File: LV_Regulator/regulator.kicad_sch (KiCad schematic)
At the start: 0 parts

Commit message: Kicad Regulator & Buck Boost controller Schematic Progress
Put down basic components and imported TI FET's & Buck-Boost Controller, as well as some of the basic connections between Controller and FET's.
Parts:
- added C1, C2: 100, symbol Device:C
- added C3: 80uF, symbol Device:C
- added C4: 40uF, symbol Device:C
- added L1: 10uH, symbol Device:L
- added R5: 133k, symbol Device:R
- added U1: BQ25858QWRRVRQ1, RRV0036B-IPC_A, symbol Controller_Library:BQ25858QWRRVRQ1
- added U2, U3, U4, U5: CSD19506KTT, DDPAK/TO-263_KTT_TEX, symbol Controller_Library:CSD19506KTT
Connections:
- new net: C1.2, U1.26 (BTST1)
- new net: C4.1, U4.2 (D)
- new net: R5.1, U1.36 (FSW_SYNC)
- new net BTST2: C2.2, U1.20 (BTST2)
- new net GND: C3.2, C4.2, R5.2, U1.10 (IIN), U1.17 (MODE), U1.37 (PGND), U1.9 (IOUT), U3.3 (S), U5.3 (S)
- new net HIDRV1_FET1_U2: U1.27 (HIDRV1), U2.1 (G)
- new net HIDRV2_FET4_U4: U1.19 (HIDRV2), U4.1 (G)
- new net LODRV1_FET2_U5: U1.25 (LODRV1), U5.1 (G)
- new net LODRV2_FET3_U3: U1.21 (LODRV2), U3.1 (G)
- new net SW1_FETs: C1.1, L1.1, U1.28 (SW1), U2.3 (S), U5.2 (D)
- new net SW2-FETs: C2.1, L1.2, U1.18 (SW2), U3.2 (D), U4.3 (S)
- new net VAC: C3.1, U2.2 (D)
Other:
- note added: "Buck-Boost Controller"
- note added: "MOSFET's & VAC wiring"

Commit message: Fixed last commit
Fixed all mistakes from the last push
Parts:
- removed C1, C2: 100, symbol Device:C
- removed C3: 80uF, symbol Device:C
- removed C4: 40uF, symbol Device:C
- added C20: 80uF, symbol Device:C
- added C21, C24: 40uF, symbol Device:C
- added C22, C23, C25, C26: 100nF, symbol Device:C
- added C27: C_Polarized, symbol Device:C_Polarized
- added R10: 5m, symbol Device:R
- added R11, R12: 10, symbol Device:R
- renumbered R5 to R13, U4 to U10, U1 to U6, U2 to U7, U5 to U8, U3 to U9
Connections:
- net VAC is gone; now on net DCIN: U7.2 (D)
- net BTST2: now also C23.1; no longer U6.20 (BTST2)
- net GND: now also R13.1, C20.2, C21.2, C24.2, C25.1, C26.2, C27.2; no longer R13.2
- net at U6.26 (BTST1): no longer names the net of U6.26 (BTST1)
- net at U10.2 (D): now also C21.1, R10.1, R11.1
- net at U6.36 (FSW_SYNC): now also R13.2; no longer R13.1
- net I2C_SCL: now reaches U6.1 (SCL)
- net VOUT: now reaches U6.12 (VO_SNS)
- net VOUT: now also C24.1, C27.1, R10.2, R12.1
- net SRN: now reaches U6.13 (SRN)
- net SRN: now also C25.2, R12.2
- net SRP: now reaches U6.14 (SRP)
- net SRP: now also C26.1, R11.2
- net I2C_SDA: now reaches U6.2 (SDA)
- net DCIN: now reaches U6.33 (VAC)
- net DCIN: now also C20.1
- net HIDRV1_FET1_U2: no longer names the net of U6.27 (HIDRV1)
- net HIDRV1_FET1_U2: no longer U7.1 (G)
- net HIDRV2_FET4_U4: no longer names the net of U6.19 (HIDRV2)
- net HIDRV2_FET4_U4: no longer U10.1 (G)
- net LODRV1_FET2_U5: no longer names the net of U6.25 (LODRV1)
- net LODRV1_FET2_U5: no longer U8.1 (G)
- net LODRV2_FET3_U3: no longer names the net of U6.21 (LODRV2)
- net LODRV2_FET3_U3: no longer U9.1 (G)
- net SW1_FETs renamed SW1
- net SW1: now also C22.2; no longer U6.28 (SW1)
- net SW2-FETs renamed SW2
- net SW2: now also C23.2; no longer U6.18 (SW2)
- new net BTST1: C22.1
- new net HIDRV1_FET1: U7.1 (G)
- new net HIDRV2_FET4: U10.1 (G)
- new net LODRV1_FET2: U8.1 (G)
- new net LODRV2_FET3: U9.1 (G)
- no-connect marks 0 -> 6
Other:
- note added: "MOSFET's & DCIN"
- note removed: "MOSFET's & VAC wiring"
- moved on the sheet: R13, U10, U6, U7, U8, U9

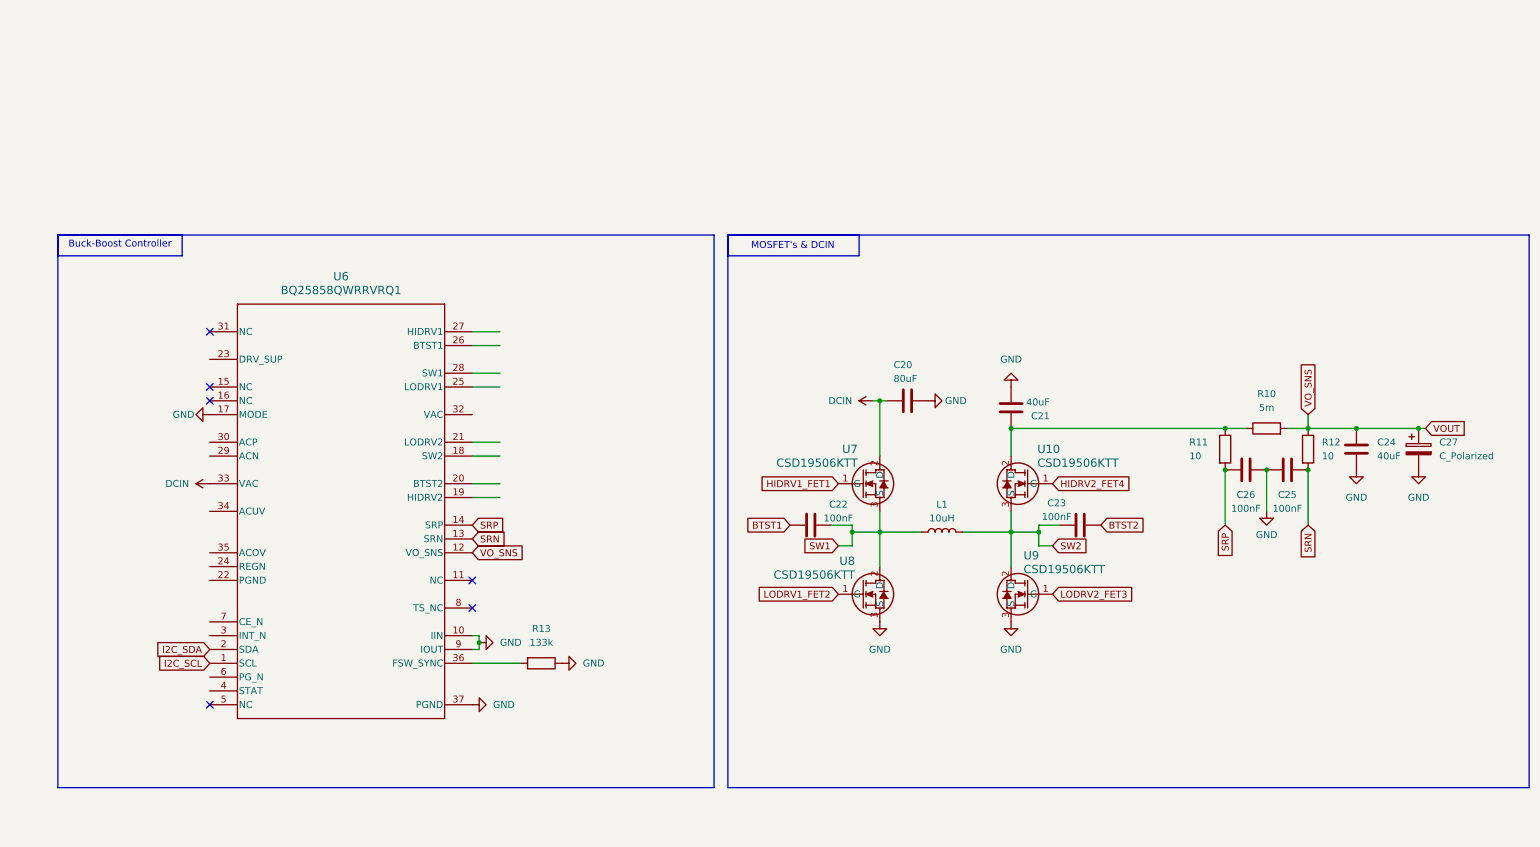
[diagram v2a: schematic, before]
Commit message: Added Start Control
Added Start Control MCU to the LV_Kontrola_Main, added hsc/lsc to LV_Regulator, fixed component numbering
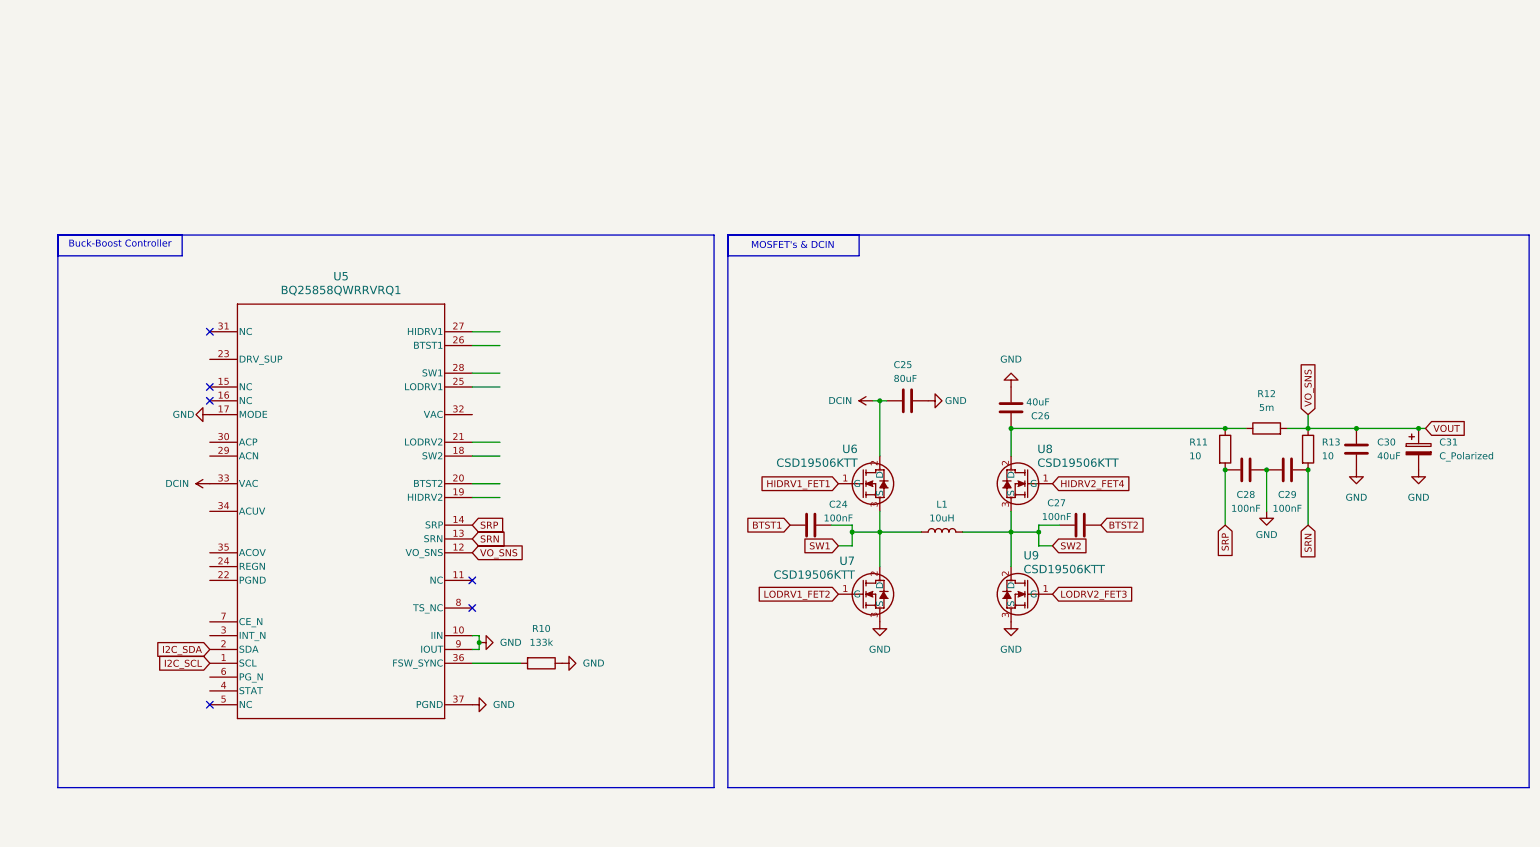
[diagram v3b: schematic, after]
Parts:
- renumbered C22 to C24, C20 to C25, C21 to C26, C23 to C27, C26 to C28, C25 to C29, C24 to C30, C27 to C31, R13 to R10, R10 to R12, R12 to R13, U6 to U5, U7 to U6, U8 to U7, U10 to U8
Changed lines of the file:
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@@
 		(dnp no)
 		(fields_autoplaced yes)
-		(property "Reference" "#PWR060"
+		(property "Reference" "#PWR066"
 			(at 44.45 99.06 0)
 			(effects
@@
 			(project ""
 				(path "/9003ce10-3354-47c9-924a-fd038a206791/7dfce8f1-0c22-480c-91d4-3ffb0e2b2dff"
-					(reference "#PWR060")
+					(reference "#PWR066")
 					(unit 1)
 				)
@@
 		(dnp no)
 		(fields_autoplaced yes)
-		(property "Reference" "#PWR059"
+		(property "Reference" "#PWR070"
 			(at 166.37 83.82 0)
 			(effects
@@
 			(project "LV_Regulator"
 				(path "/9003ce10-3354-47c9-924a-fd038a206791/7dfce8f1-0c22-480c-91d4-3ffb0e2b2dff"
-					(reference "#PWR059")
+					(reference "#PWR070")
 					(unit 1)
 				)
@@
 		(on_board yes)
 		(dnp no)
-		(property "Reference" "C21"
+		(property "Reference" "C26"
 			(at 195.072 86.614 0)
 			(effects
@@
 			(project "LV_Regulator"
 				(path "/9003ce10-3354-47c9-924a-fd038a206791/7dfce8f1-0c22-480c-91d4-3ffb0e2b2dff"
-					(reference "C21")
+					(reference "C26")
 					(unit 1)
 				)
@@
 		(dnp no)
 		(fields_autoplaced yes)
-		(property "Reference" "#PWR072"
+		(property "Reference" "#PWR073"
 			(at 187.96 74.93 0)
 			(effects
@@
 			(project "LV_Regulator"
 				(path "/9003ce10-3354-47c9-924a-fd038a206791/7dfce8f1-0c22-480c-91d4-3ffb0e2b2dff"
-					(reference "#PWR072")
+					(reference "#PWR073")
 					(unit 1)
 				)
@@
 		(on_board yes)
 		(dnp no)
-		(property "Reference" "U8"
+		(property "Reference" "U7"
 			(at 159.258 113.284 0)
 			(effects
@@
 			(project "LV_Regulator"
 				(path "/9003ce10-3354-47c9-924a-fd038a206791/7dfce8f1-0c22-480c-91d4-3ffb0e2b2dff"
-					(reference "U8")
+					(reference "U7")
 					(unit 1)
 				)
@@
 		(dnp no)
 		(fields_autoplaced yes)
-		(property "Reference" "R10"
+		(property "Reference" "R12"
 			(at 234.95 82.55 90)
 			(effects
@@
 			(project ""
 				(path "/9003ce10-3354-47c9-924a-fd038a206791/7dfce8f1-0c22-480c-91d4-3ffb0e2b2dff"
-					(reference "R10")
+					(reference "R12")
 					(unit 1)
 				)
@@
 		(on_board yes)
 		(dnp no)
-		(property "Reference" "C27"
+		(property "Reference" "C31"
 			(at 266.7 91.44 0)
 			(effects
@@
 			(project ""
 				(path "/9003ce10-3354-47c9-924a-fd038a206791/7dfce8f1-0c22-480c-91d4-3ffb0e2b2dff"
-					(reference "C27")
+					(reference "C31")
 					(unit 1)
 				)
@@
 		(on_board yes)
 		(dnp no)
-		(property "Reference" "#PWR063"
+		(property "Reference" "#PWR075"
 			(at 234.95 110.49 0)
 			(effects
@@
 			(project "LV_Regulator"
 				(path "/9003ce10-3354-47c9-924a-fd038a206791/7dfce8f1-0c22-480c-91d4-3ffb0e2b2dff"
-					(reference "#PWR063")
+					(reference "#PWR075")
 					(unit 1)
 				)
@@
 		(on_board yes)
 		(dnp no)
-		(property "Reference" "C20"
+		(property "Reference" "C25"
 			(at 166.37 77.216 90)
 			(effects
@@
 			(project ""
 				(path "/9003ce10-3354-47c9-924a-fd038a206791/7dfce8f1-0c22-480c-91d4-3ffb0e2b2dff"
-					(reference "C20")
+					(reference "C25")
 					(unit 1)
 				)
@@
 		(dnp no)
 		(fields_autoplaced yes)
-		(property "Reference" "#PWR068"
+		(property "Reference" "#PWR067"
 			(at 95.25 139.7 0)
 			(effects
@@
 			(project "LV_Regulator"
 				(path "/9003ce10-3354-47c9-924a-fd038a206791/7dfce8f1-0c22-480c-91d4-3ffb0e2b2dff"
-					(reference "#PWR068")
+					(reference "#PWR067")
 					(unit 1)
 				)
@@
 		(on_board yes)
 		(dnp no)
-		(property "Reference" "U10"
+		(property "Reference" "U8"
 			(at 192.786 92.71 0)
 			(effects
@@
 			(project "LV_Regulator"
 				(path "/9003ce10-3354-47c9-924a-fd038a206791/7dfce8f1-0c22-480c-91d4-3ffb0e2b2dff"
-					(reference "U10")
+					(reference "U8")
 					(unit 1)
 				)
@@
 		(on_board yes)
 		(dnp no)
-		(property "Reference" "#PWR066"
+		(property "Reference" "#PWR065"
 			(at 34.29 86.36 0)
 			(effects
@@
 			(project "LV_Regulator"
 				(path "/9003ce10-3354-47c9-924a-fd038a206791/7dfce8f1-0c22-480c-91d4-3ffb0e2b2dff"
-					(reference "#PWR066")
+					(reference "#PWR065")
 					(unit 1)
 				)
@@
 		(dnp no)
 		(fields_autoplaced yes)
-		(property "Reference" "#PWR062"
+		(property "Reference" "#PWR076"
 			(at 251.46 102.87 0)
 			(effects
@@
 			(project "LV_Regulator"
 				(path "/9003ce10-3354-47c9-924a-fd038a206791/7dfce8f1-0c22-480c-91d4-3ffb0e2b2dff"
-					(reference "#PWR062")
+					(reference "#PWR076")
 					(unit 1)
 				)
@@
 		(dnp no)
 		(fields_autoplaced yes)
-		(property "Reference" "R13"
+		(property "Reference" "R10"
 			(at 101.6 125.73 90)
 			(effects
@@
 			(project "LV_Regulator"
 				(path "/9003ce10-3354-47c9-924a-fd038a206791/7dfce8f1-0c22-480c-91d4-3ffb0e2b2dff"
-					(reference "R13")
+					(reference "R10")
 					(unit 1)
 				)
@@
 		(dnp no)
 		(fields_autoplaced yes)
-		(property "Reference" "#PWR070"
+		(property "Reference" "#PWR071"
 			(at 163.83 130.81 0)
 			(effects
@@
 			(project "LV_Regulator"
 				(path "/9003ce10-3354-47c9-924a-fd038a206791/7dfce8f1-0c22-480c-91d4-3ffb0e2b2dff"
-					(reference "#PWR070")
+					(reference "#PWR071")
 					(unit 1)
 				)
@@
 		(on_board yes)
 		(dnp no)
-		(property "Reference" "C23"
+		(property "Reference" "C27"
 			(at 196.342 102.616 90)
 			(effects
@@
 			(project "LV_Regulator"
 				(path "/9003ce10-3354-47c9-924a-fd038a206791/7dfce8f1-0c22-480c-91d4-3ffb0e2b2dff"
-					(reference "C23")
+					(reference "C27")
 					(unit 1)
 				)
@@
 		(dnp no)
 		(fields_autoplaced yes)
-		(property "Reference" "U6"
+		(property "Reference" "U5"
 			(at 64.77 60.96 0)
 			(effects
@@
 			(project "LV_Regulator"
 				(path "/9003ce10-3354-47c9-924a-fd038a206791/7dfce8f1-0c22-480c-91d4-3ffb0e2b2dff"
-					(reference "U6")
+					(reference "U5")
 					(unit 1)
 				)
@@
 		(on_board yes)
 		(dnp no)
-		(property "Reference" "C22"
+		(property "Reference" "C24"
 			(at 156.21 102.87 90)
 			(effects
@@
 			(project "LV_Regulator"
 				(path "/9003ce10-3354-47c9-924a-fd038a206791/7dfce8f1-0c22-480c-91d4-3ffb0e2b2dff"
-					(reference "C22")
+					(reference "C24")
 					(unit 1)
 				)
@@
 		(dnp no)
 		(fields_autoplaced yes)
-		(property "Reference" "C24"
+		(property "Reference" "C30"
 			(at 255.27 91.4399 0)
 			(effects
@@
 			(project ""
 				(path "/9003ce10-3354-47c9-924a-fd038a206791/7dfce8f1-0c22-480c-91d4-3ffb0e2b2dff"
-					(reference "C24")
+					(reference "C30")
 					(unit 1)
 				)
@@
 		(on_board yes)
 		(dnp no)
-		(property "Reference" "C26"
+		(property "Reference" "C28"
 			(at 231.14 101.092 90)
 			(effects
@@
 			(project "LV_Regulator"
 				(path "/9003ce10-3354-47c9-924a-fd038a206791/7dfce8f1-0c22-480c-91d4-3ffb0e2b2dff"
-					(reference "C26")
+					(reference "C28")
 					(unit 1)
 				)
@@
 		(dnp no)
 		(fields_autoplaced yes)
-		(property "Reference" "R12"
+		(property "Reference" "R13"
 			(at 245.11 91.4399 0)
 			(effects
@@
 			(project "LV_Regulator"
 				(path "/9003ce10-3354-47c9-924a-fd038a206791/7dfce8f1-0c22-480c-91d4-3ffb0e2b2dff"
-					(reference "R12")
+					(reference "R13")
 					(unit 1)
 				)
@@
 		(dnp no)
 		(fields_autoplaced yes)
-		(property "Reference" "#PWR061"
+		(property "Reference" "#PWR077"
 			(at 262.89 102.87 0)
 			(effects
@@
 			(project ""
 				(path "/9003ce10-3354-47c9-924a-fd038a206791/7dfce8f1-0c22-480c-91d4-3ffb0e2b2dff"
-					(reference "#PWR061")
+					(reference "#PWR077")
 					(unit 1)
 				)
@@
 		(on_board yes)
 		(dnp no)
-		(property "Reference" "C25"
+		(property "Reference" "C29"
 			(at 238.76 101.092 90)
 			(effects
@@
 			(project "LV_Regulator"
 				(path "/9003ce10-3354-47c9-924a-fd038a206791/7dfce8f1-0c22-480c-91d4-3ffb0e2b2dff"
-					(reference "C25")
+					(reference "C29")
 					(unit 1)
 				)
@@
 		(on_board yes)
 		(dnp no)
-		(property "Reference" "#PWR071"
+		(property "Reference" "#PWR072"
 			(at 179.07 83.82 0)
 			(effects
@@
 			(project "LV_Regulator"
 				(path "/9003ce10-3354-47c9-924a-fd038a206791/7dfce8f1-0c22-480c-91d4-3ffb0e2b2dff"
-					(reference "#PWR071")
+					(reference "#PWR072")
 					(unit 1)
 				)
@@
 		(on_board yes)
 		(dnp no)
-		(property "Reference" "U7"
+		(property "Reference" "U6"
 			(at 159.766 92.71 0)
 			(effects
@@
 			(project "LV_Regulator"
 				(path "/9003ce10-3354-47c9-924a-fd038a206791/7dfce8f1-0c22-480c-91d4-3ffb0e2b2dff"
-					(reference "U7")
+					(reference "U6")
 					(unit 1)
 				)
@@
 		(dnp no)
 		(fields_autoplaced yes)
-		(property "Reference" "#PWR067"
+		(property "Reference" "#PWR068"
 			(at 96.52 128.27 0)
 			(effects
@@
 			(project "LV_Regulator"
 				(path "/9003ce10-3354-47c9-924a-fd038a206791/7dfce8f1-0c22-480c-91d4-3ffb0e2b2dff"
-					(reference "#PWR067")
+					(reference "#PWR068")
 					(unit 1)
 				)
@@
 		(dnp no)
 		(fields_autoplaced yes)
-		(property "Reference" "#PWR073"
+		(property "Reference" "#PWR074"
 			(at 187.96 130.81 0)
 			(effects
@@
 			(project "LV_Regulator"
 				(path "/9003ce10-3354-47c9-924a-fd038a206791/7dfce8f1-0c22-480c-91d4-3ffb0e2b2dff"
-					(reference "#PWR073")
-					(unit 1)
-				)
+					(reference "#PWR074")
+					(unit 1)
+				)

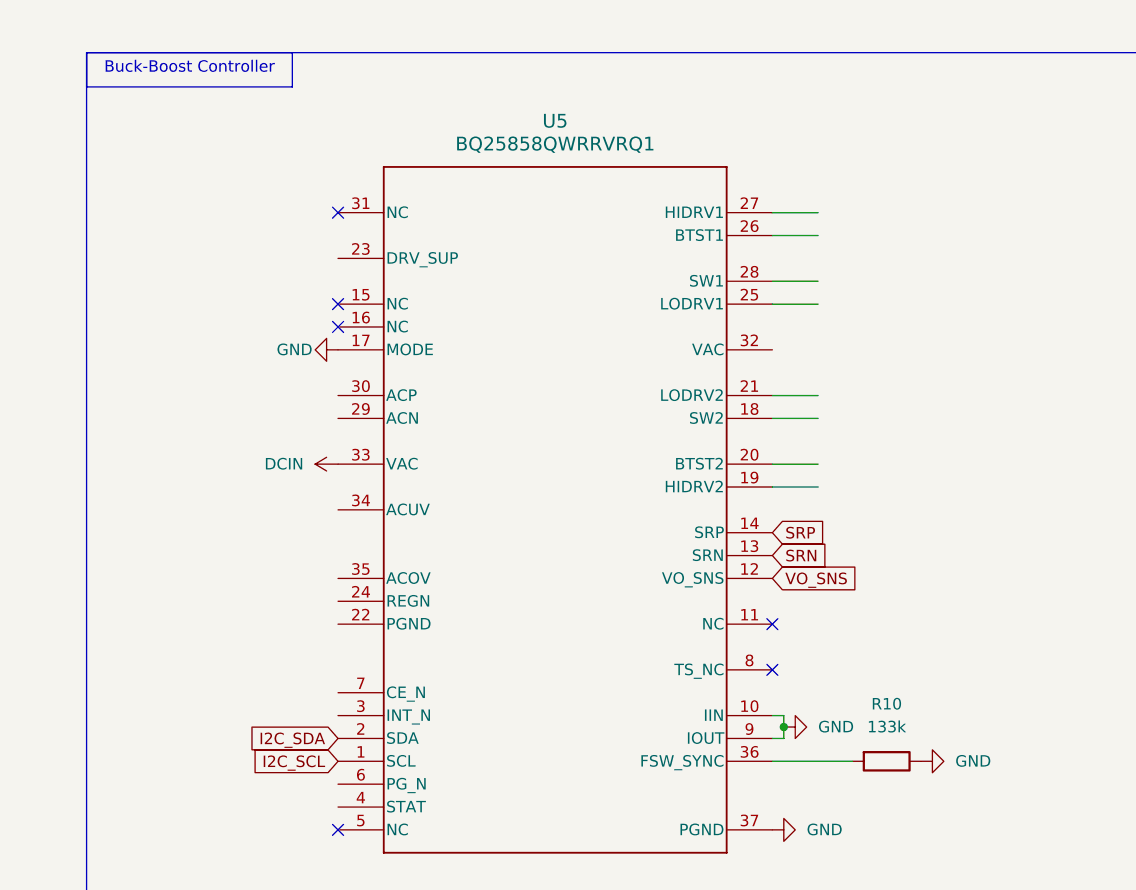
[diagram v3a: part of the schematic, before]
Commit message: Continuation of BQ25858 Schematic drawing
Added more components from the examples schematic provided from TI.
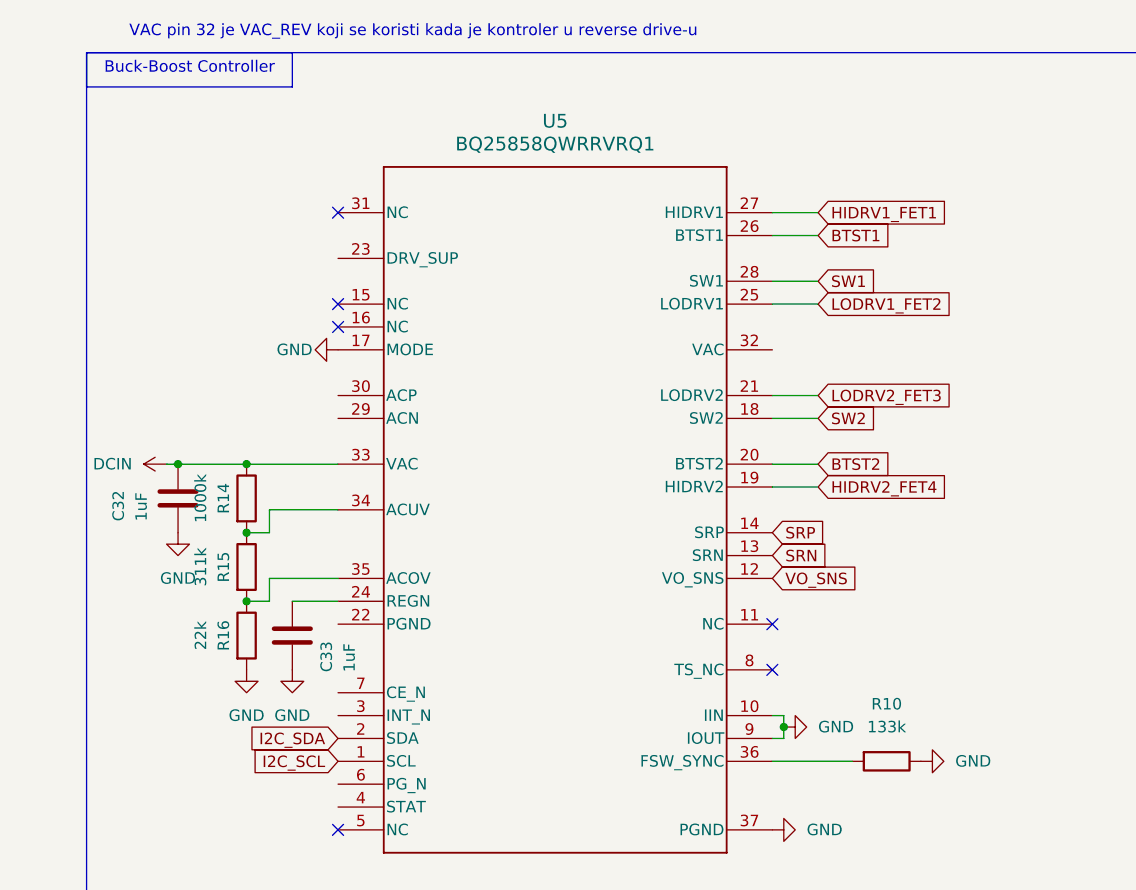
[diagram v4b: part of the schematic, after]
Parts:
- added C32, C33: 1uF, symbol Device:C
- added R14: 1000k, symbol Device:R
- added R15: 311k, symbol Device:R
- added R16: 22k, symbol Device:R
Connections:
- net BTST1: now also U5.26 (BTST1)
- net BTST2: now also U5.20 (BTST2)
- net DCIN: now also C32.2, R14.1
- net GND: now also C32.1, C33.1, R16.2
- net HIDRV1_FET1: now also U5.27 (HIDRV1)
- net HIDRV2_FET4: now also U5.19 (HIDRV2)
- net LODRV1_FET2: now also U5.25 (LODRV1)
- net LODRV2_FET3: now also U5.21 (LODRV2)
- net SW1: now also U5.28 (SW1)
- net SW2: now also U5.18 (SW2)
- net at U5.24 (REGN): now also C33.2
- net at U5.34 (ACUV): now also R14.2, R15.1
- net at U5.35 (ACOV): now also R15.2, R16.1
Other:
- note added: "VAC pin 32 je VAC_REV koji se koristi kada je kontroler u reverse drive-u"
